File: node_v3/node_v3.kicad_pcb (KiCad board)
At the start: 2 copper layers, 45.7 x 76.2 mm, 36 parts, among them J1 Conn_Coaxial, J10 Conn_01x02_Pin, J11 Conn_01x02_Pin, J12 USB_BOOT', J13 Conn_01x03_Pin, J14 Conn_01x02_Pin, J2 Micro_SD_Card, J3 Conn_01x02_Pin, J4 Conn_01x02_Pin, J5 Conn_01x04_Pin, J6 Conn_01x02_Pin, J7 Conn_01x06_Pin, J8 Conn_01x04_Pin, J9 Conn_01x03_Pin, U1 RFM69HCW, U3 MCP73831-2-OT, U4 ADP2108AUJ-3.3, U5 CAT3200-5, U6 RP2040, U7 W25Q128JVS

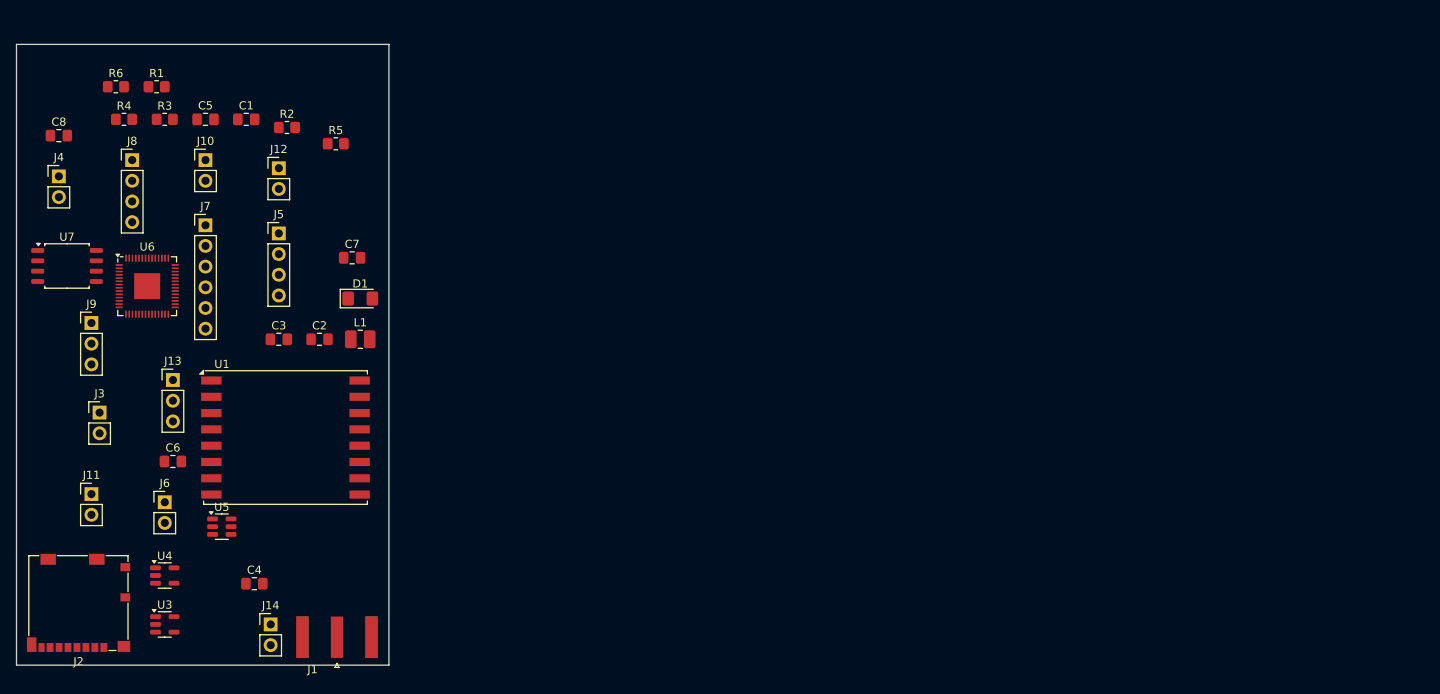
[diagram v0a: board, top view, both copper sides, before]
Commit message: moved stuff around, replaced headers, usb, footprints, started pcb
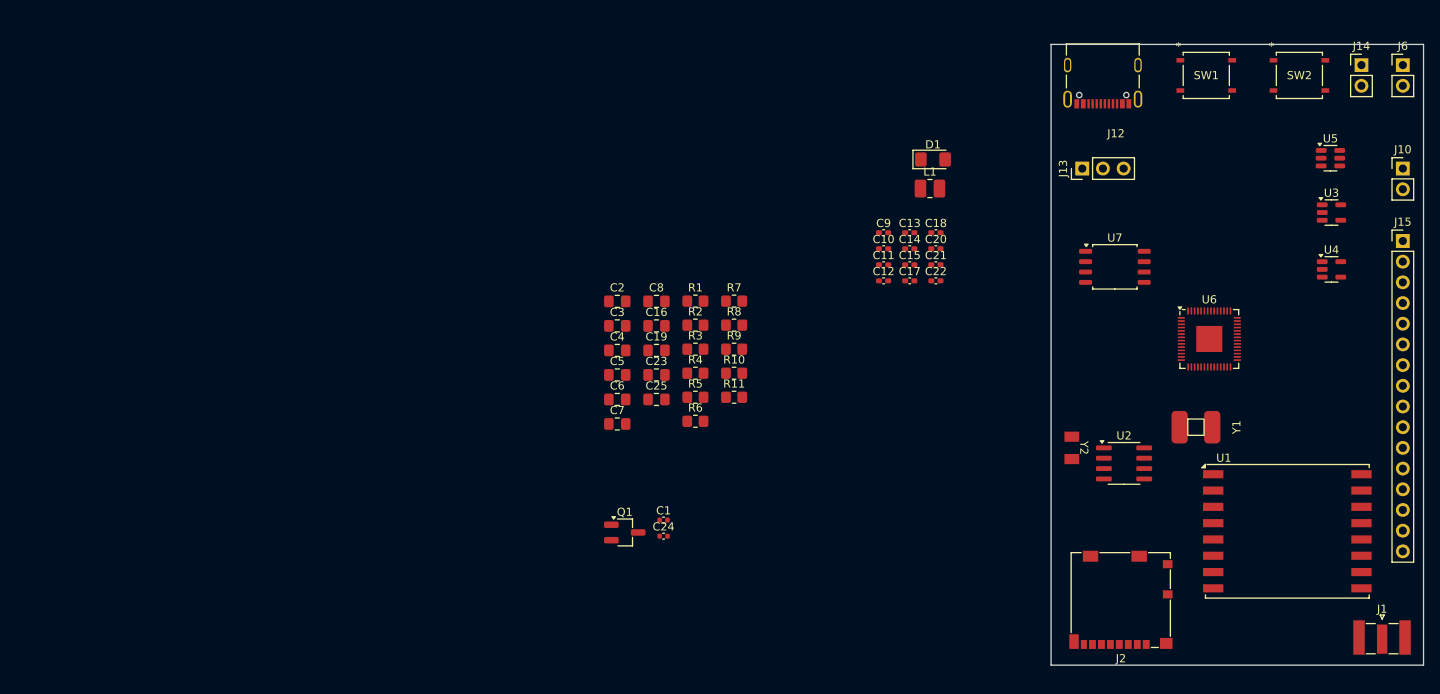
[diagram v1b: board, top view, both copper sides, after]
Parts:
- removed J11, J3, J4: Conn_01x02_Pin, Connector_PinHeader_2.54mm:PinHeader_1x02_P2.54mm_Vertical
- removed J5, J8: Conn_01x04_Pin, Connector_PinHeader_2.54mm:PinHeader_1x04_P2.54mm_Vertical
- removed J7: Conn_01x06_Pin, Connector_PinHeader_2.54mm:PinHeader_1x06_P2.54mm_Vertical
- removed J9: Conn_01x03_Pin, Connector_PinHeader_2.54mm:PinHeader_1x03_P2.54mm_Vertical
- added C10: 100n, Capacitor_SMD:C_0402_1005Metric_Pad0.74x0.62mm_HandSolder, F.Cu at (157.2, 75.9)
- added C11: 100n, Capacitor_SMD:C_0402_1005Metric_Pad0.74x0.62mm_HandSolder, F.Cu at (157.2, 77.9)
- added C12: 100n, Capacitor_SMD:C_0402_1005Metric_Pad0.74x0.62mm_HandSolder, F.Cu at (157.2, 79.8)
- added C13: 100n, Capacitor_SMD:C_0402_1005Metric_Pad0.74x0.62mm_HandSolder, F.Cu at (160.4, 73.9)
- added C14: 100n, Capacitor_SMD:C_0402_1005Metric_Pad0.74x0.62mm_HandSolder, F.Cu at (160.4, 75.9)
- added C15: 100n, Capacitor_SMD:C_0402_1005Metric_Pad0.74x0.62mm_HandSolder, F.Cu at (160.4, 77.9)
- added C16: 1u, Capacitor_SMD:C_0805_2012Metric_Pad1.18x1.45mm_HandSolder, F.Cu at (129.4, 85.4)
- added C17: 100n, Capacitor_SMD:C_0402_1005Metric_Pad0.74x0.62mm_HandSolder, F.Cu at (160.4, 79.8)
- added C18: 100n, Capacitor_SMD:C_0402_1005Metric_Pad0.74x0.62mm_HandSolder, F.Cu at (163.7, 73.9)
- added C19: 1u, Capacitor_SMD:C_0805_2012Metric_Pad1.18x1.45mm_HandSolder, F.Cu at (129.4, 88.4)
- added C20: 100n, Capacitor_SMD:C_0402_1005Metric_Pad0.74x0.62mm_HandSolder, F.Cu at (163.7, 75.9)
- added C21: 15p, Capacitor_SMD:C_0402_1005Metric_Pad0.74x0.62mm_HandSolder, F.Cu at (163.7, 77.9)
- added C22: 15p, Capacitor_SMD:C_0402_1005Metric_Pad0.74x0.62mm_HandSolder, F.Cu at (163.7, 79.8)
- added C23: 10u, Capacitor_SMD:C_0805_2012Metric_Pad1.18x1.45mm_HandSolder, F.Cu at (129.4, 91.4)
- added C24: .1u, Capacitor_SMD:C_0402_1005Metric, F.Cu at (130.2, 111.2)
- added C25: 10u, Capacitor_SMD:C_0805_2012Metric_Pad1.18x1.45mm_HandSolder, F.Cu at (129.4, 94.4)
- added C9: 100n, Capacitor_SMD:C_0402_1005Metric_Pad0.74x0.62mm_HandSolder, F.Cu at (157.2, 73.9)
- added J15: Conn_01x16_Pin, Connector_PinHeader_2.54mm:PinHeader_1x16_P2.54mm_Vertical, F.Cu at (221.0, 74.9)
- added Q1: 2N3904, Package_TO_SOT_SMD:SC-59_Handsoldering, F.Cu at (125.5, 110.7)
- added R10: 1k, Resistor_SMD:R_0805_2012Metric_Pad1.20x1.40mm_HandSolder, F.Cu at (138.9, 91.2)
- added R11: 0, Resistor_SMD:R_0805_2012Metric_Pad1.20x1.40mm_HandSolder, F.Cu at (138.9, 94.1)
- added R7: 27.4, Resistor_SMD:R_0805_2012Metric_Pad1.20x1.40mm_HandSolder, F.Cu at (138.9, 82.3)
- added R8: 27.4, Resistor_SMD:R_0805_2012Metric_Pad1.20x1.40mm_HandSolder, F.Cu at (138.9, 85.3)
- added R9: DNF, Resistor_SMD:R_0805_2012Metric_Pad1.20x1.40mm_HandSolder, F.Cu at (138.9, 88.2)
- added SW1: PTS526, custom:PTS526, F.Cu at (196.8, 54.6)
- added SW2: PTS526, custom:PTS526, F.Cu at (208.3, 54.6)
- added U2: MCP7940N-xSN, Package_SO:SOIC-8_3.9x4.9mm_P1.27mm, F.Cu at (186.8, 102.2)
- added Y1: 445C35A12M00000, kicad-footprints-master:XTAL_M445, F.Cu at (195.6, 97.8)
- added Y2: SC32S-7PF20PPM, custom:SC-32S, F.Cu at (180.3, 100.3)
- C1: footprint Capacitor_SMD:C_0805_2012Metric_Pad1.18x1.45mm_HandSolder -> Capacitor_SMD:C_0402_1005Metric
- J1: footprint Connector_Coaxial:SMA_Amphenol_132289_EdgeMount -> Connector_Coaxial:SMA_Samtec_SMA-J-P-X-ST-EM1_EdgeMount
- J10: value Conn_01x02_Pin -> 3V3OUT
- J12: value USB_BOOT' -> 12402012E212A; footprint Connector_PinHeader_2.54mm:PinHeader_1x02_P2.54mm_Vertical -> custom:AMPHENOL_12402012E212A
- J13: value Conn_01x03_Pin -> DBG
- J14: value Conn_01x02_Pin -> VIN
- J6: value Conn_01x02_Pin -> BAT
- moved J6 161.2 mm to (221.0, 53.3)
- moved U3 151.9 mm to (212.2, 71.4)
- moved J14 150.5 mm to (215.9, 53.3)
- moved U4 148.1 mm to (212.2, 78.4)
- moved J10 147.0 mm to (221.0, 66.0)
- moved U5 143.4 mm to (212.1, 64.8)
- moved U6 130.5 mm to (197.2, 87.0)
- moved U7 128.6 mm to (185.6, 78.1)
- moved J1 128.3 mm to (218.4, 123.6), turned to 0 degrees
- moved J2 128.0 mm to (186.4, 119.0)
- moved U1 123.5 mm to (206.8, 110.6)
- moved J13 114.6 mm to (181.6, 66.0), turned to 90 degrees
- moved J12 101.9 mm to (184.2, 53.3), turned to 180 degrees
- moved R6 82.1 mm to (134.1, 97.1)
- moved R4 76.8 mm to (134.1, 91.2)
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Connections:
- J2 pad 9: unconnected-(J2-SHIELD-Pad9) -> GND
- U6 pad 15: EXT_BTN -> EXT_SW1
- U6 pad 16: EXT_SW -> EXT_SW2
- U6 pad 18: unconnected-(U6-GPIO15-Pad18) -> RTC_MFP
- U6 pad 26: unconnected-(U6-RUN-Pad26) -> Net-(U6-RUN)

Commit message: finished? the pcb design - need to look into sd card stuff first
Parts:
- added BT1: Battery_Cell, custom:BAT-HLD-001-THM_TEC, B.Cu at (98.4, 85.2)
- added C26: 6p, Capacitor_SMD:C_0603_1608Metric_Pad1.08x0.95mm_HandSolder, F.Cu at (103.1, 87.0)
- added C27: 6p, Capacitor_SMD:C_0603_1608Metric_Pad1.08x0.95mm_HandSolder, F.Cu at (105.6, 87.0)
- moved J6 157.5 mm to (63.5, 54.8), turned to 90 degrees
- moved J14 152.5 mm to (63.5, 50.0), turned to 90 degrees
- moved J10 146.0 mm to (75.8, 50.0), turned to 90 degrees
- moved SW2 144.1 mm to (64.4, 62.7), turned to 90 degrees
- moved U5 135.1 mm to (77.2, 57.5), turned to 90 degrees
- moved SW1 133.9 mm to (64.4, 74.1), turned to 90 degrees
- moved J12 125.6 mm to (63.1, 86.8), turned to -90 degrees
- moved U3 124.8 mm to (88.0, 59.0), turned to 90 degrees
- moved U6 120.1 mm to (77.7, 75.0), turned to 90 degrees
- moved U4 113.7 mm to (100.1, 59.3), turned to 90 degrees
- moved Y1 111.7 mm to (86.0, 76.0), turned to 90 degrees
- moved J1 110.2 mm to (134.2, 52.5), turned to 90 degrees
- moved J13 104.0 mm to (80.0, 88.1), turned to 180 degrees
- moved J15 102.1 mm to (122.0, 50.0), turned to -90 degrees
- moved U1 98.1 mm to (120.4, 64.2), turned to 90 degrees
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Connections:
- Q1 pad 1: 5V_SW -> 5V_OUT
- U1 pad 10: GND -> (no net)
- U2 pad 3: RTC_BAT -> Net-(BT1-+)
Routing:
- net 3V3: track 0.00 -> 227.2 mm, vias 0 -> 6
- net MISO: track 0.00 -> 93.7 mm, vias 0 -> 3
- net SPI_SCK: track 0.00 -> 87.5 mm, vias 0 -> 1
- net MOSI: track 0.00 -> 85.6 mm, vias 0 -> 5
- net VIN: track 0.00 -> 80.2 mm
- net UART_RX: track 0.00 -> 75.5 mm, vias 0 -> 1
- net BAT: track 0.00 -> 71.8 mm
- net UART_TX: track 0.00 -> 68.0 mm, vias 0 -> 1
- net SD_CS: track 0.00 -> 62.5 mm, vias 0 -> 2
- net I2C_SDA: track 0.00 -> 60.4 mm, vias 0 -> 1
- net I2C_SCK: track 0.00 -> 59.2 mm, vias 0 -> 3
- net 5V_SW: track 0.00 -> 56.7 mm, vias 0 -> 2
- net Net-(BT1-+): track 0.00 -> 50.4 mm
- net RFM_RST: track 0.00 -> 47.7 mm
- net RFM_CS: track 0.00 -> 45.4 mm
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- added copper zone on B.Cu, net GND
- added copper zone on F.Cu, net GND
- added copper zone on In2.Cu, net Net-(J12-SHIELD)
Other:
- board size 45.7 x 76.2 mm -> 76.2 x 45.7 mm
- copper layers 2 -> 4
- board text added: "100n"
- board text added: "3V3"
- board text added: "ADP2108"
- board text added: "BAT"
- board text added: "BOOTSEL"
- board text added: "CAT3200"
- board text added: "CLK"
- board text added: "CR2032"
- board text added: "GND"
- board text added: "GND 3V3"
- board text added: "MCP73831"
- board text added: "MCP7940"
- board text added: "QSPI FLASH"
- board text added: "RESET"
- board text added: "RFM69HCW"
- board text added: "RP2040"
- board text added: "SD CARD"
- board text added: "SMA"
- board text added: "SW1 SW2 GP6 GP26 GP27 MISO MOSI SPI_SCK SPI_CS I2C_SDA I2C_SCK TX RX 5V SW 3V3 GND"
- board text added: "SWD"
- board text added: "USB 2.0"
- board text added: "VIN"
- board text added: "WiSDOM Node v3.0 March 2024 By Amelia Vlahogiannis"

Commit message: not finished yet
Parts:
- added R12: R, Resistor_SMD:R_0805_2012Metric_Pad1.20x1.40mm_HandSolder, F.Cu at (127.3, 76.4)
- added R13: R, Resistor_SMD:R_0805_2012Metric_Pad1.20x1.40mm_HandSolder, F.Cu at (118.7, 91.3)
- added R14: R, Resistor_SMD:R_0805_2012Metric_Pad1.20x1.40mm_HandSolder, F.Cu at (115.9, 86.8)
- added R15: R, Resistor_SMD:R_0805_2012Metric_Pad1.20x1.40mm_HandSolder, F.Cu at (114.9, 91.2)
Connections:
- BT1 pad 2: Net-(BT1-+) -> GND
- BT1 pad 3: Net-(BT1-+) -> (no net)
- BT1 pad 4: Net-(BT1-+) -> (no net)
- J2 pad 1: GND -> Net-(J2-DAT2)
- J2 pad 8: GND -> Net-(J2-DAT1)
- U1 pad 10: (no net) -> GND
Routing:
- net 3V3: track 227.2 -> 256.1 mm, vias 6 -> 9
- net Net-(J2-DAT1): track 0.00 -> 24.1 mm, vias 0 -> 2
- net SD_CS: track 62.5 -> 81.6 mm, vias 2 -> 3
- net Net-(J2-DAT2): track 0.00 -> 10.5 mm
- net MISO: track 93.7 -> 102.3 mm, vias 3 -> 5
- net GND: vias 51 -> 49

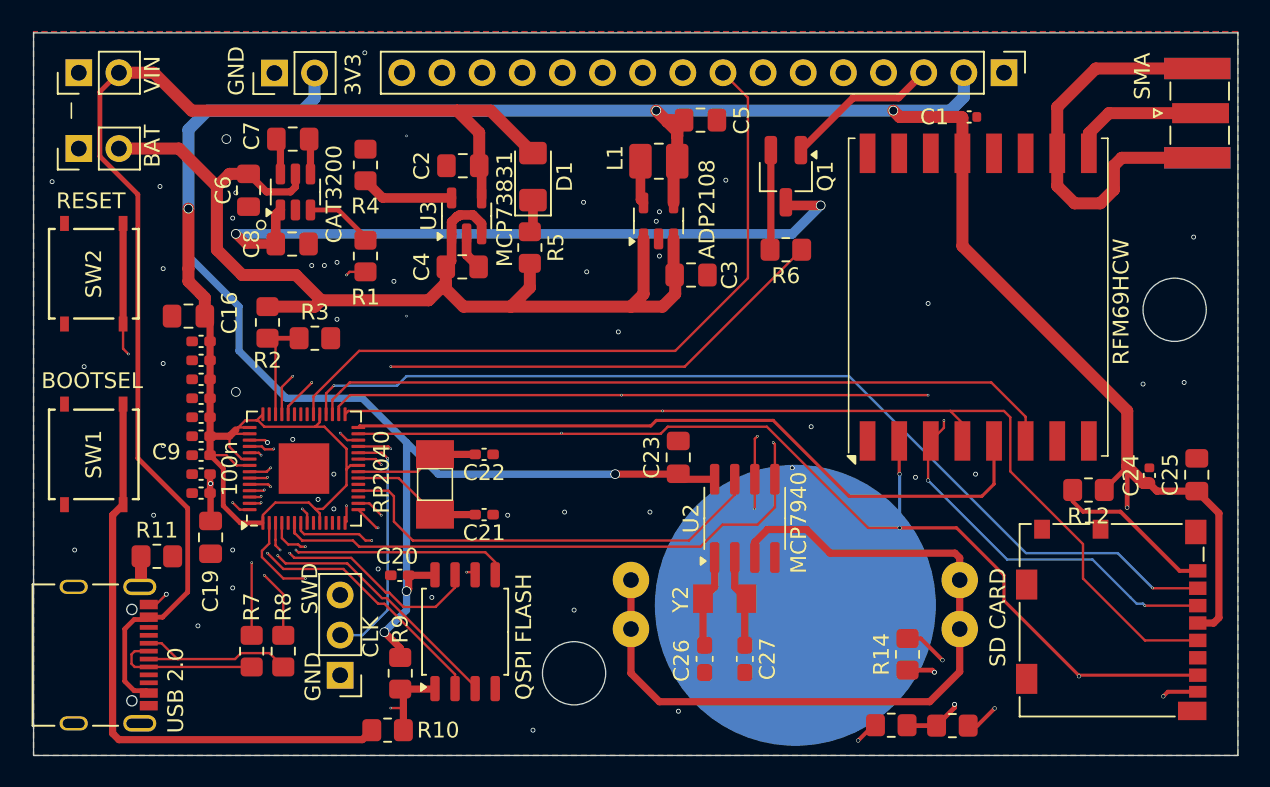
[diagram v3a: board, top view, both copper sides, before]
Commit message: fixed the rfm footprint, fixed via sizes. need to adjust some vias to be bigger
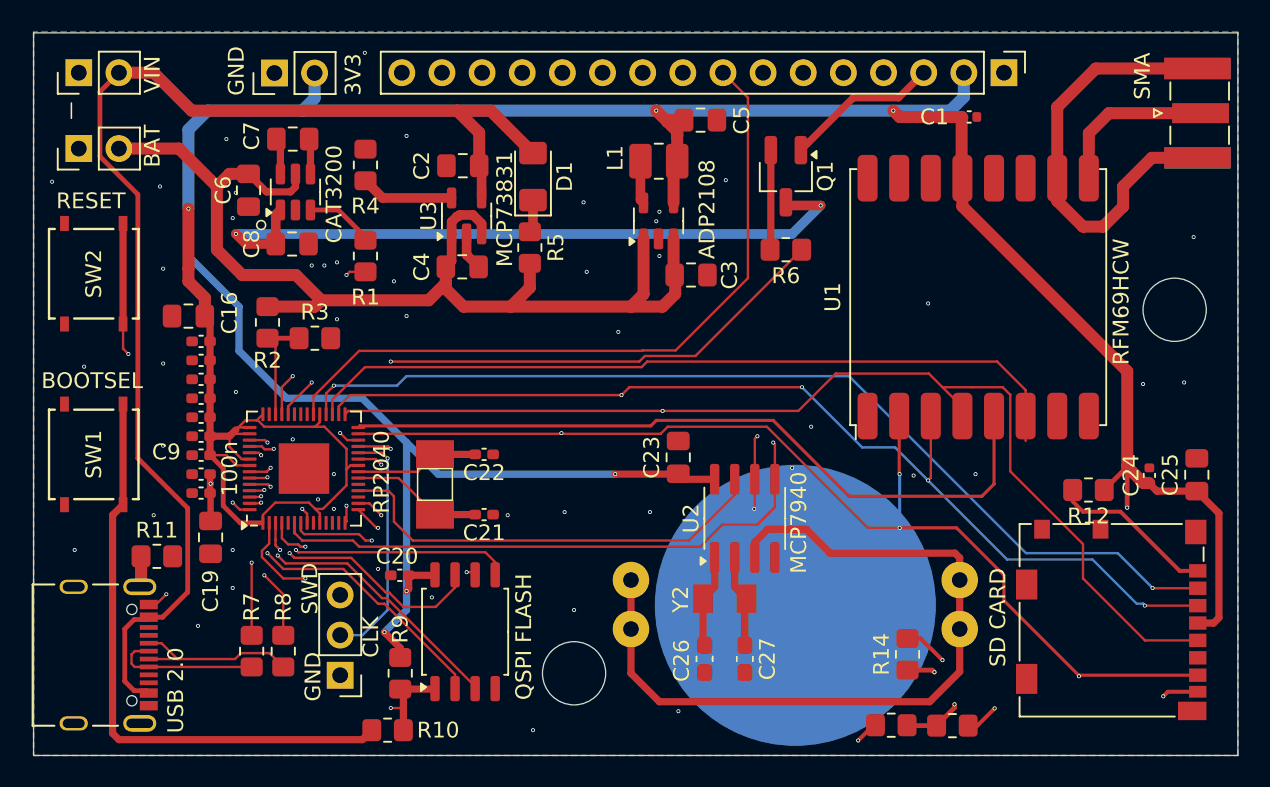
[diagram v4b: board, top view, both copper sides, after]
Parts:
- U1: footprint RF_Module:HOPERF_RFM69HW -> RF_Module:HOPERF_RFM9XW_SMD
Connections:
- BT1 pad 5: GND -> (no net)
- J15 pad 3: 5V_SW -> 5V_OUT
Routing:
- net 5V_OUT: track 0.00 -> 9.80 mm
- net 5V_SW: track 56.7 -> 47.1 mm
- net SPI_SCK: track 87.5 -> 91.6 mm
- net RFM_RST: track 47.7 -> 49.7 mm
- net GND: track 30.1 -> 31.7 mm
- net RFM_CS: track 45.4 -> 47.0 mm
- net MISO: track 102.3 -> 103.8 mm
- net MOSI: track 85.6 -> 86.5 mm, vias 5 -> 4
